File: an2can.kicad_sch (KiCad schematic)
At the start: 18 parts, among them J1 PWR/CAN, U1 MAX6025, U2 Tex_DCDC_v2

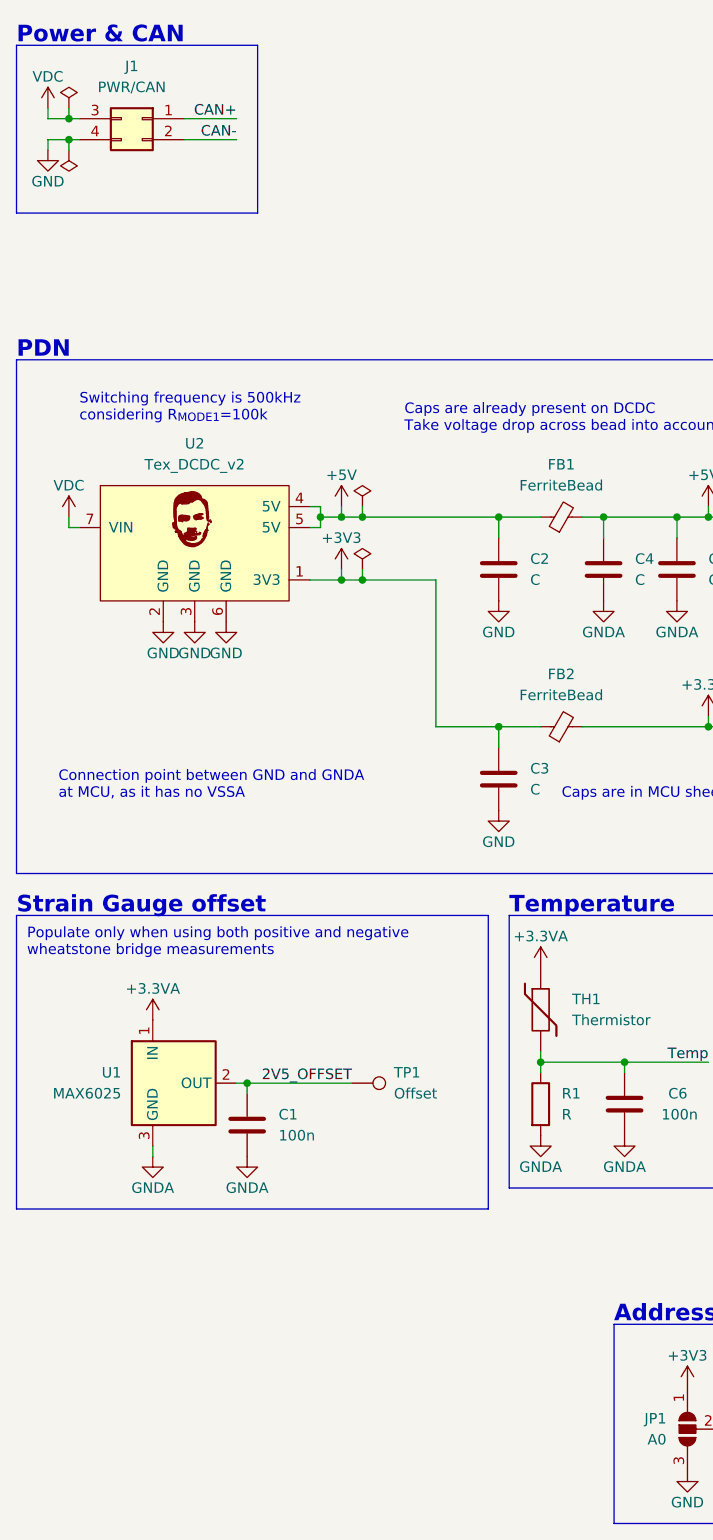
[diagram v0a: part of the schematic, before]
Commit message: pcb: complete routing, add silkscreen details, finalize board
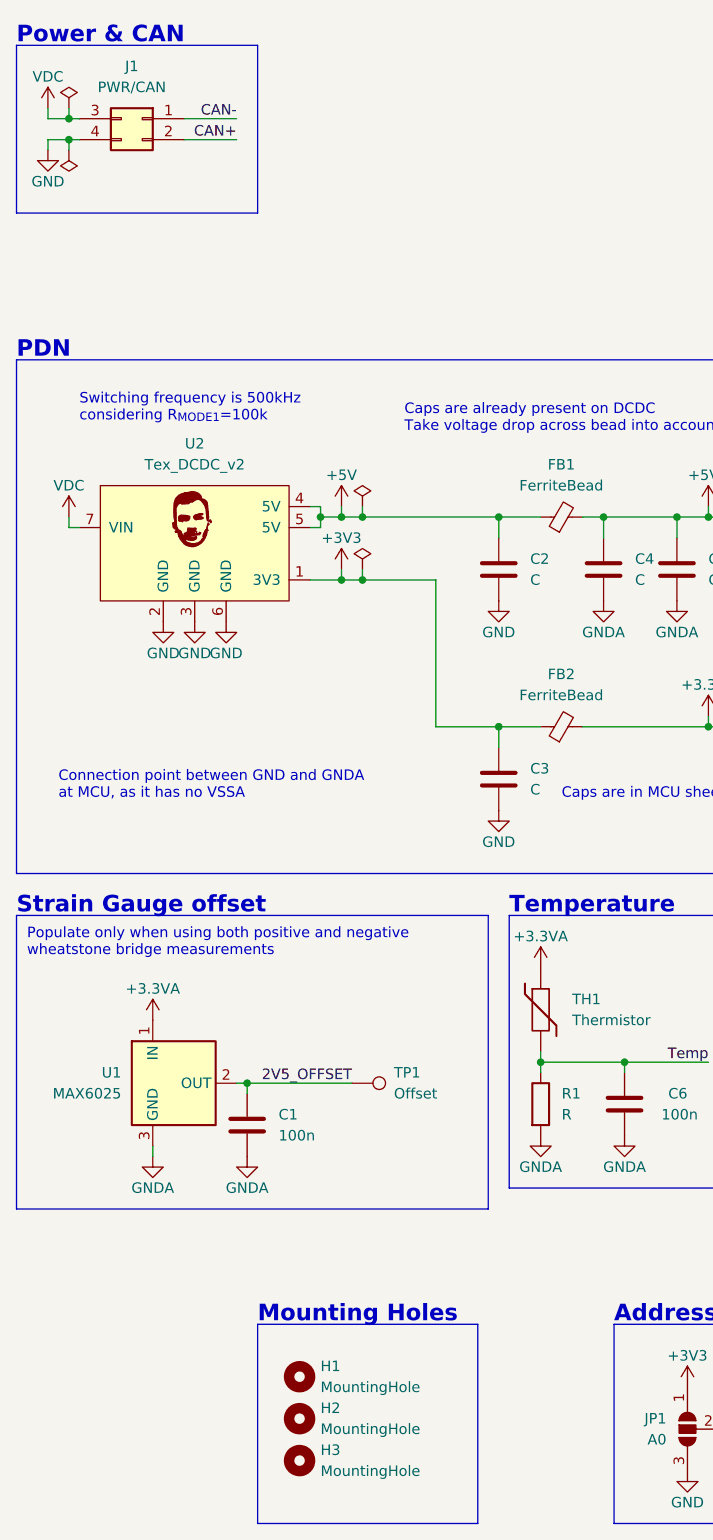
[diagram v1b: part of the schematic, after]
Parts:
- added H1, H2, H3: MountingHole, Eagle_Main:MountingHole_3.2mm_M3_ISO14580, symbol Mechanical:MountingHole
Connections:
- net CAN+: now also J1.2 (Pin_2); no longer J1.1 (Pin_1)
- net CAN-: now also J1.1 (Pin_1); no longer J1.2 (Pin_2)
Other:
- note added: "Mounting Holes"
